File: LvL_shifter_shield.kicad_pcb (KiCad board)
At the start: 4 copper layers, 43.2 x 17.8 mm, 10 parts, among them J1 Conn_02x08_Counter_Clockwise, J2 Conn_01x15_Socket, J3 Conn_01x15_Socket, J4 Power, U1 TXB0108DQSR, U2 TXB0108DQSR

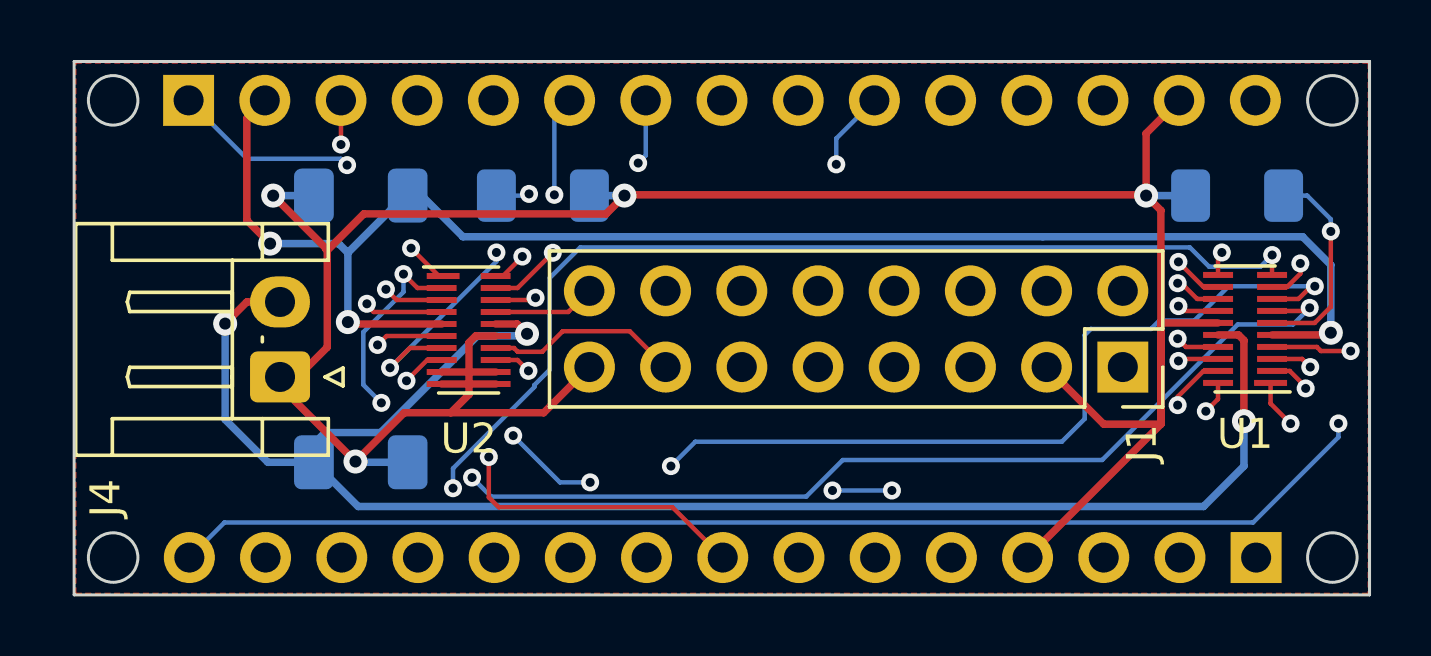
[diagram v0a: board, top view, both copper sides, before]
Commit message: Updated silkscreen and added a +5 link to the nano
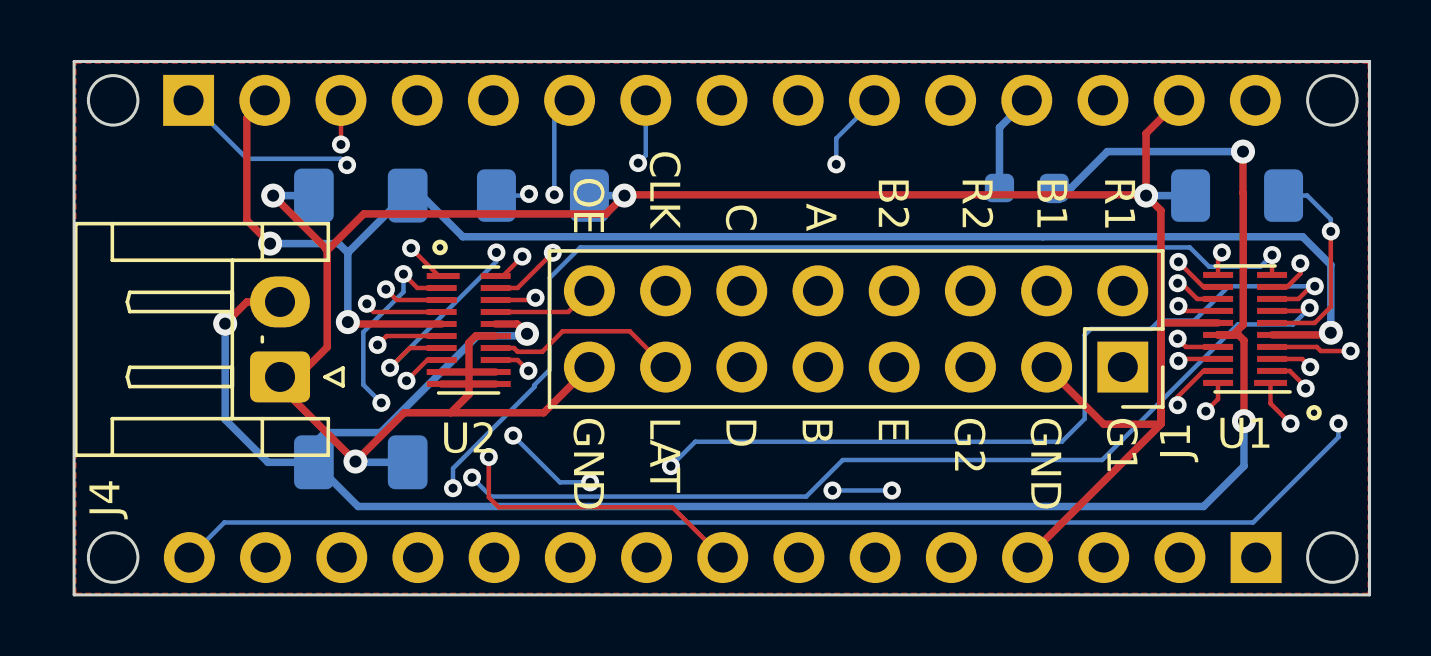
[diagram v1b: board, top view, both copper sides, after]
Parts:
- added R3: r=0, Resistor_SMD:R_0603_1608Metric_Pad0.98x0.95mm_HandSolder, B.Cu at (134.0, 81.0)
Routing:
- net +5V: track 56.6 -> 70.6 mm, vias 3 -> 4
- net /+5V2: track 0.00 -> 3.30 mm
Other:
- board text added: "+3.3V"
- board text added: "+5V"
- board text added: "A"
- board text added: "B"
- board text added: "B1"
- board text added: "B2"
- board text added: "C"
- board text added: "CLK"
- board text added: "D"
- board text added: "E"
- board text added: "G1"
- board text added: "G2"
- board text added: "GND"
- board text added: "LAT"
- board text added: "OE"
- board text added: "R1"
- board text added: "R2"

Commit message: Forgot to set OE high when power is connected
You can work around this with a jumper wire from 3.3v to the OE side of the R1 and R2
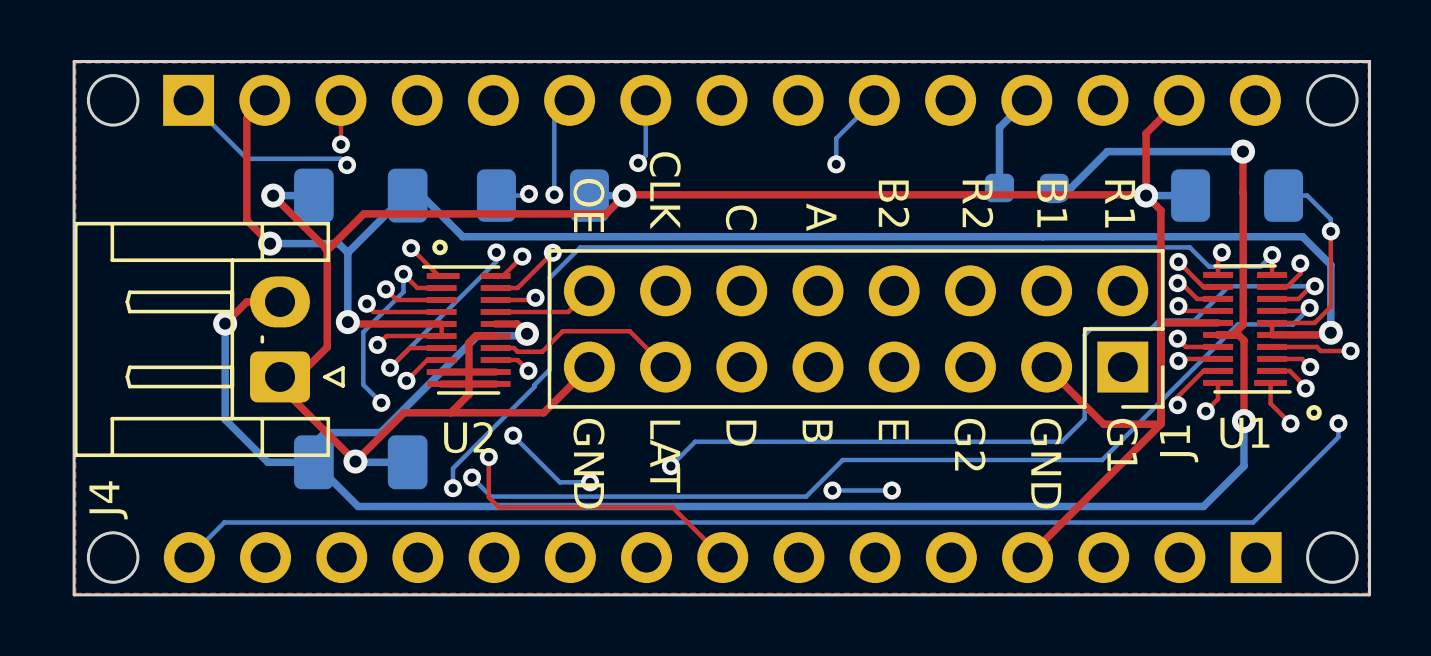
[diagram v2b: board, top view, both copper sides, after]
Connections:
- R1 pad 2: Net-(U1-OE) -> +3.3V
- R2 pad 2: Net-(U2-OE) -> +3.3V
- U1 pad 6: Net-(U1-OE) -> +3.3V
- U2 pad 6: Net-(U2-OE) -> +3.3V
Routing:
- net +3.3V: track 52.3 -> 71.8 mm, vias 3 -> 6
- net Net-(U2-OE): track 11.5 -> 0.00 mm, vias 2 -> 0
- net Net-(U1-OE): track 7.00 -> 0.00 mm, vias 1 -> 0
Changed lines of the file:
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@@
   (net 43 "/RESET2")
   (net 44 "/+5V2")
-  (net 45 "Net-(U1-OE)")
-  (net 46 "Net-(U2-OE)")
   (footprint "Package_SON:USON-20_2x4mm_P0.4mm" (layer "F.Cu")
     (at 141.235 85.725 180)
@@
       (net 3 "+3.3V") (pinfunction "VCCA") (pintype "power_in"))
     (pad "6" smd rect (at -0.9 0.2 90) (size 0.2 1) (layers "F.Cu" "F.Paste" "F.Mask")
-      (net 45 "Net-(U1-OE)") (pinfunction "OE") (pintype "input"))
+      (net 3 "+3.3V") (pinfunction "OE") (pintype "input"))
     (pad "7" smd rect (at -0.9 0.6 90) (size 0.2 1) (layers "F.Cu" "F.Paste" "F.Mask")
       (net 41 "/PA16") (pinfunction "A5") (pintype "bidirectional"))
@@
       (net 3 "+3.3V") (pinfunction "VCCA") (pintype "power_in"))
     (pad "6" smd rect (at -0.9 0.2 270) (size 0.2 1) (layers "F.Cu" "F.Paste" "F.Mask")
-      (net 46 "Net-(U2-OE)") (pinfunction "OE") (pintype "input"))
+      (net 3 "+3.3V") (pinfunction "OE") (pintype "input"))
     (pad "7" smd rect (at -0.9 0.6 270) (size 0.2 1) (layers "F.Cu" "F.Paste" "F.Mask")
       (net 22 "/PA11") (pinfunction "A5") (pintype "bidirectional"))
@@
       (net 2 "GND") (pintype "passive"))
     (pad "2" smd roundrect (at 1.55 0 180) (size 1.3 1.75) (layers "B.Cu" "B.Paste" "B.Mask") (roundrect_rratio 0.1923076923)
-      (net 46 "Net-(U2-OE)") (pintype "passive"))
+      (net 3 "+3.3V") (pintype "passive"))
     (model "${KICAD6_3DMODEL_DIR}/Resistor_SMD.3dshapes/R_1206_3216Metric.wrl"
       (offset (xyz 0 0 0))
@@
       (net 2 "GND") (pintype "passive"))
     (pad "2" smd roundrect (at 1.55 0) (size 1.3 1.75) (layers "B.Cu" "B.Paste" "B.Mask") (roundrect_rratio 0.1923076923)
-      (net 45 "Net-(U1-OE)") (pintype "passive"))
+      (net 3 "+3.3V") (pintype "passive"))
     (model "${KICAD6_3DMODEL_DIR}/Resistor_SMD.3dshapes/R_1206_3216Metric.wrl"
       (offset (xyz 0 0 0))
@@
   (segment (start 111.6076 90.17) (end 113.3225 90.17) (width 0.25) (layer "B.Cu") (net 2))
   (segment (start 108.839 81.28) (end 110.1975 81.28) (width 0.25) (layer "B.Cu") (net 2))
+  (segment (start 144.0942 84.9884) (end 143.5576 85.525) (width 0.15) (layer "F.Cu") (net 3))
+  (segment (start 112.6172 85.96) (end 112.3188 86.2584) (width 0.15) (layer "F.Cu") (net 3))
   (segment (start 107.961032 78.703568) (end 107.961032 82.103832) (width 0.25) (layer "F.Cu") (net 3))
   (segment (start 111.3918 85.56) (end 114.455 85.56) (width 0.25) (layer "F.Cu") (net 3))
+  (segment (start 112.3188 86.2584) (end 112.0902 86.2584) (width 0.15) (layer "F.Cu") (net 3))
+  (segment (start 114.455 85.96) (end 112.6172 85.96) (width 0.15) (layer "F.Cu") (net 3))
+  (segment (start 114.455 85.96) (end 114.455 85.56) (width 0.15) (layer "F.Cu") (net 3))
   (segment (start 144.0942 85.852) (end 144.0212 85.925) (width 0.25) (layer "F.Cu") (net 3))
   (segment (start 144.0212 85.925) (end 142.135 85.925) (width 0.25) (layer "F.Cu") (net 3))
+  (segment (start 143.5576 85.525) (end 142.135 85.525) (width 0.15) (layer "F.Cu") (net 3))
   (segment (start 111.3282 85.4964) (end 111.3918 85.56) (width 0.25) (layer "F.Cu") (net 3))
+  (segment (start 142.135 85.525) (end 142.135 85.925) (width 0.15) (layer "F.Cu") (net 3))
+  (segment (start 144.0942 82.4738) (end 144.0942 84.9884) (width 0.15) (layer "F.Cu") (net 3))
   (segment (start 108.5596 78.105) (end 107.961032 78.703568) (width 0.25) (layer "F.Cu") (net 3))
   (segment (start 107.961032 82.103832) (end 108.7374 82.8802) (width 0.25) (layer "F.Cu") (net 3))
   (via (at 108.7374 82.8802) (size 0.8) (drill 0.4) (layers "F.Cu" "B.Cu") (net 3))
+  (via (at 117.368077 81.223877) (size 0.6) (drill 0.3) (layers "F.Cu" "B.Cu") (net 3))
+  (via (at 144.0942 82.4738) (size 0.6) (drill 0.3) (layers "F.Cu" "B.Cu") (net 3))
   (via (at 144.0942 85.852) (size 0.8) (drill 0.4) (layers "F.Cu" "B.Cu") (net 3))
   (via (at 111.3282 85.4964) (size 0.8) (drill 0.4) (layers "F.Cu" "B.Cu") (net 3))
+  (via (at 112.3188 86.2584) (size 0.6) (drill 0.3) (layers "F.Cu" "B.Cu") (net 3))
+  (segment (start 115.4176 83.174354) (end 115.4176 84.836) (width 0.15) (layer "In1.Cu") (net 3))
+  (segment (start 113.03 85.5472) (end 112.3188 86.2584) (width 0.15) (layer "In1.Cu") (net 3))
+  (segment (start 115.4176 84.836) (end 114.7064 85.5472) (width 0.15) (layer "In1.Cu") (net 3))
+  (segment (start 117.368077 81.223877) (end 115.4176 83.174354) (width 0.15) (layer "In1.Cu") (net 3))
+  (segment (start 114.7064 85.5472) (end 113.03 85.5472) (width 0.15) (layer "In1.Cu") (net 3))
+  (segment (start 117.311954 81.28) (end 116.28 81.28) (width 0.15) (layer "B.Cu") (net 3))
   (segment (start 108.7374 82.8802) (end 111.0234 82.8802) (width 0.25) (layer "B.Cu") (net 3))
+  (segment (start 144.0942 82.4738) (end 144.0942 82.0674) (width 0.15) (layer "B.Cu") (net 3))
   (segment (start 115.1636 82.6516) (end 134.493 82.6516) (width 0.25) (layer "B.Cu") (net 3))
   (segment (start 111.0234 82.8802) (end 111.3282 83.185) (width 0.25) (layer "B.Cu") (net 3))
@@
   (segment (start 144.0942 83.5914) (end 144.0942 85.852) (width 0.25) (layer "B.Cu") (net 3))
   (segment (start 113.792 81.28) (end 115.1636 82.6516) (width 0.25) (layer "B.Cu") (net 3))
+  (segment (start 143.3068 81.28) (end 142.52 81.28) (width 0.15) (layer "B.Cu") (net 3))
+  (segment (start 117.368077 81.223877) (end 117.311954 81.28) (width 0.15) (layer "B.Cu") (net 3))
   (segment (start 134.493 82.6516) (end 143.1544 82.6516) (width 0.25) (layer "B.Cu") (net 3))
+  (segment (start 144.0942 82.0674) (end 143.3068 81.28) (width 0.15) (layer "B.Cu") (net 3))
   (segment (start 139.1762 85.125) (end 139.0142 84.963) (width 0.15) (layer "F.Cu") (net 4))
   (segment (start 140.335 85.125) (end 139.1762 85.125) (width 0.15) (layer "F.Cu") (net 4))
@@
   (segment (start 133.049 79.0156) (end 133.9596 78.105) (width 0.25) (layer "B.Cu") (net 44))
   (segment (start 133.049 81.026) (end 133.049 79.0156) (width 0.25) (layer "B.Cu") (net 44))
-  (segment (start 144.0942 84.9884) (end 143.5576 85.525) (width 0.15) (layer "F.Cu") (net 45))
-  (segment (start 143.5576 85.525) (end 142.135 85.525) (width 0.15) (layer "F.Cu") (net 45))
-  (segment (start 144.0942 82.4738) (end 144.0942 84.9884) (width 0.15) (layer "F.Cu") (net 45))
-  (via (at 144.0942 82.4738) (size 0.6) (drill 0.3) (layers "F.Cu" "B.Cu") (net 45))
-  (segment (start 144.0942 82.4738) (end 144.0942 82.0674) (width 0.15) (layer "B.Cu") (net 45))
-  (segment (start 143.3068 81.28) (end 142.52 81.28) (width 0.15) (layer "B.Cu") (net 45))
-  (segment (start 144.0942 82.0674) (end 143.3068 81.28) (width 0.15) (layer "B.Cu") (net 45))
-  (segment (start 112.6172 85.96) (end 112.3188 86.2584) (width 0.15) (layer "F.Cu") (net 46))
-  (segment (start 114.455 85.96) (end 112.6172 85.96) (width 0.15) (layer "F.Cu") (net 46))
-  (via (at 117.368077 81.223877) (size 0.6) (drill 0.3) (layers "F.Cu" "B.Cu") (net 46))
-  (via (at 112.3188 86.2584) (size 0.6) (drill 0.3) (layers "F.Cu" "B.Cu") (net 46))
-  (segment (start 115.4176 83.174354) (end 115.4176 84.836) (width 0.15) (layer "In1.Cu") (net 46))
-  (segment (start 113.03 85.5472) (end 112.3188 86.2584) (width 0.15) (layer "In1.Cu") (net 46))
-  (segment (start 115.4176 84.836) (end 114.7064 85.5472) (width 0.15) (layer "In1.Cu") (net 46))
-  (segment (start 117.368077 81.223877) (end 115.4176 83.174354) (width 0.15) (layer "In1.Cu") (net 46))
-  (segment (start 114.7064 85.5472) (end 113.03 85.5472) (width 0.15) (layer "In1.Cu") (net 46))
-  (segment (start 117.311954 81.28) (end 116.28 81.28) (width 0.15) (layer "B.Cu") (net 46))
-  (segment (start 117.368077 81.223877) (end 117.311954 81.28) (width 0.15) (layer "B.Cu") (net 46))
   (zone (net 2) (net_name "GND") (layer "F.Cu") (hatch edge 0.5)
     (connect_pads (clearance 0.5))

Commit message: Updated version number, added open hardware logo
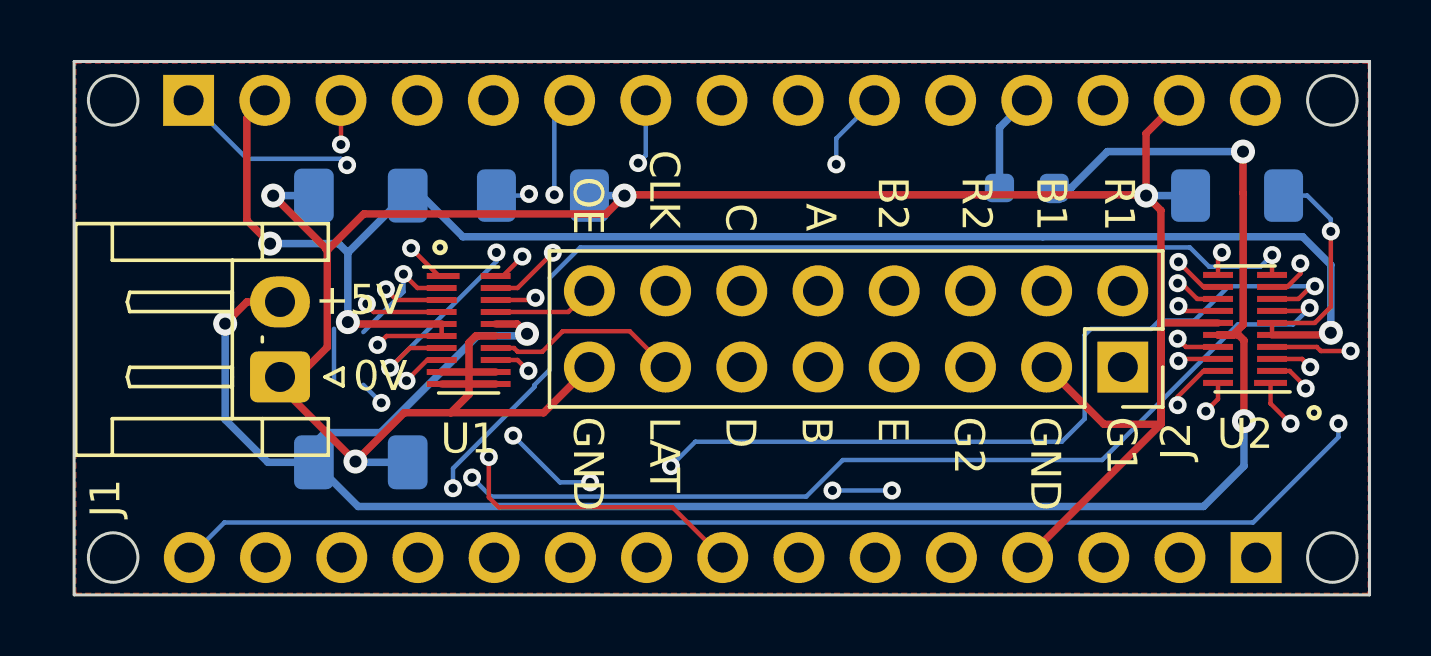
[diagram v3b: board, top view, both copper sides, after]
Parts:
- added REF**: OSHW-Symbol_6.7x6mm_SilkScreen, Symbol:OSHW-Symbol_6.7x6mm_SilkScreen, B.Cu at (114.3, 85.6)
- renumbered C2 to C1, C1 to C2, J4 to J1, J1 to J2, J2 to J3, J3 to J4, U2 to U1, U1 to U2
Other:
- board text added: "0V"
- board text added: "nano33iot_hub75e_hat_v1.3"
- board text removed: "nano33_hub75e_hat_v1.2"

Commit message: switched pin PA03 and PA02, added internal 5V
the dip switch can be used to get external 5v, internal or when none is selected the usb 5v from the arduino
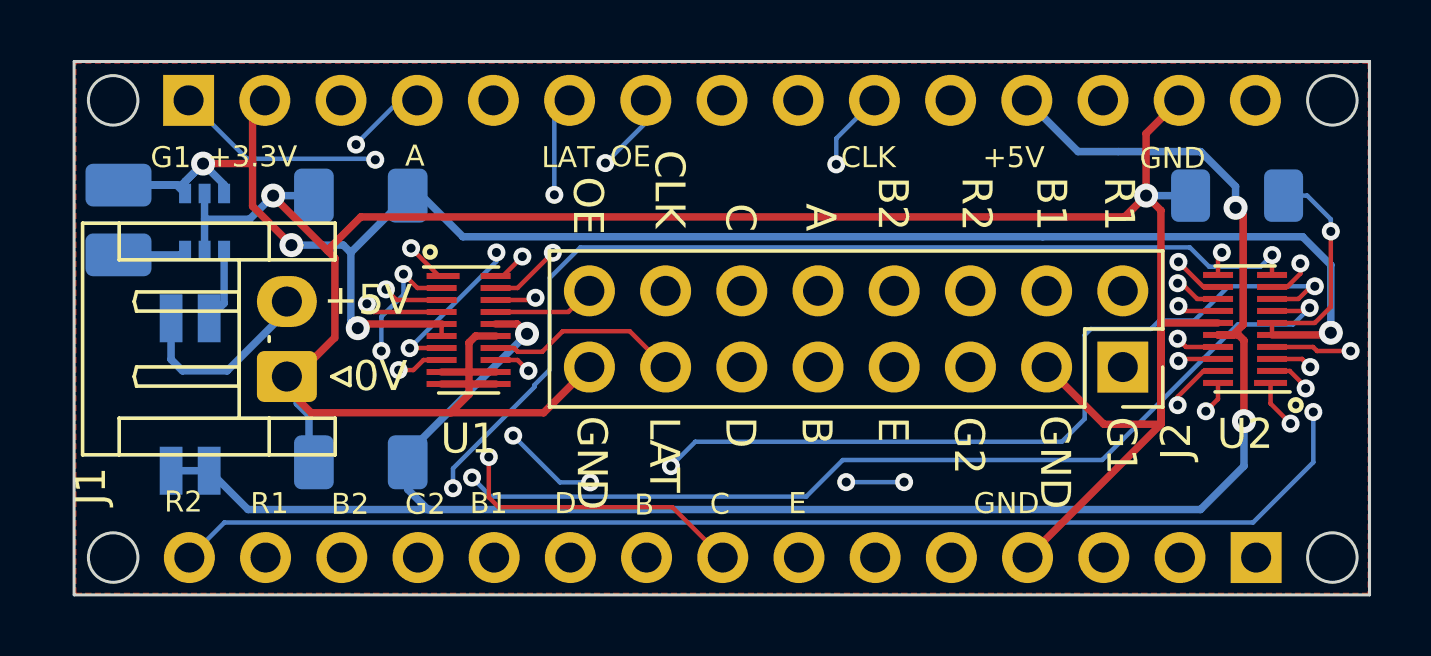
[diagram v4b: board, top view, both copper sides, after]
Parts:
- removed R2: r=100k, Resistor_SMD:R_1206_3216Metric_Pad1.30x1.75mm_HandSolder
- removed R3: r=0, Resistor_SMD:R_0603_1608Metric_Pad0.98x0.95mm_HandSolder
- added L1: 10u, Inductor_SMD:L_1008_2520Metric_Pad1.43x2.20mm_HandSolder, B.Cu at (103.7, 82.1)
- added SW1: SW_DIP_x02, Button_Switch_SMD:SW_DIP_SPSTx02_Slide_Copal_CHS-02A_W5.08mm_P1.27mm_JPin, B.Cu at (106.1, 87.9)
- added U3: LTC3525-5, Package_TO_SOT_SMD:SOT-363_SC-70-6, B.Cu at (106.6, 82.2)
- C1: value 0.1u -> 10u
- C2: value 0.1u -> 22u
- moved REF** 27.8 mm to (142.1, 85.4)
- moved J1 0.23 mm to (109.3, 87.3)
- turned C2 to 180 degrees
- turned R1 to 180 degrees
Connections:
- J1 pad 2: +5V -> Net-(J1-Pin_2)
- J3 pad 12: /+5V2 -> +5V
- R1 pad 1: GND -> +3.3V
- R1 pad 2: +3.3V -> GND
- U1 pad 1: /PA03 -> /PA02
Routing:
- net /PA02: track 0.00 -> 16.3 mm, vias 0 -> 2
- net /PA03: track 14.8 -> 0.00 mm, vias 2 -> 0
- net Net-(J1-Pin_2): track 0.00 -> 6.68 mm
- net +5V: track 70.6 -> 64.9 mm, vias 4 -> 3
- net GND: track 91.4 -> 94.9 mm, vias 4 -> 2
- net /+5V2: track 3.30 -> 0.00 mm
- net +3.3V: track 71.8 -> 69.2 mm, vias 6 -> 5
- net Net-(U3-VOUT): track 0.00 -> 2.47 mm
- net Net-(U3-SW): track 0.00 -> 2.28 mm
- net /PA11: track 14.0 -> 12.2 mm
- net /PA05: track 20.9 -> 19.9 mm
- net /PA10: track 17.3 -> 16.6 mm
- net /PA19: track 48.1 -> 47.5 mm
- net /PA06: track 11.8 -> 12.3 mm
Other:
- board text added: "int 5V ext 5V"
- board text added: "nano33iot_hub75e_hat_v1.4"
- board text removed: "nano33iot_hub75e_hat_v1.3"

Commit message: fixed drill files
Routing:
- net GND: track 94.9 -> 101.5 mm, vias 2 -> 8
